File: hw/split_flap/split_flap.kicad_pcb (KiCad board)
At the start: 2 copper layers, 104.5 x 98.3 mm, 59 parts, among them J1 Conn_01x02, J10 Conn_01x05, J11 Conn_01x05, J12 Conn_01x05, J13 Conn_01x05, J14 Conn_01x05, J15 Conn_01x05, J16 Conn_01x05, J17 EXPANDER_PORT, J18 Conn_01x05, J19 POWER, J2 Conn_01x02, J20 Conn_01x05, J21 Conn_01x05, J22 Conn_01x05, J25 Conn_01x02, J26 Conn_01x02, J27 Conn_01x02, J28 Conn_01x02, J3 Conn_01x02, J4 Conn_01x02, J5 Conn_01x02, J6 Conn_01x02, J7 Conn_01x02, J8 Conn_01x02, J9 Conn_01x05, U1 PCF8574, U10 ULN2803A, U11 PCF8574, U12 ULN2803A, U13 PCF8574, U14 ULN2803A, U15 PCF8574, U2 NodeMCU_1.0_(ESP-12E), U3 PCF8574, U4 ULN2803A, U5 PCF8574, U6 ULN2803A, U7 PCF8574, U8 ULN2803A, U9 PCF8574

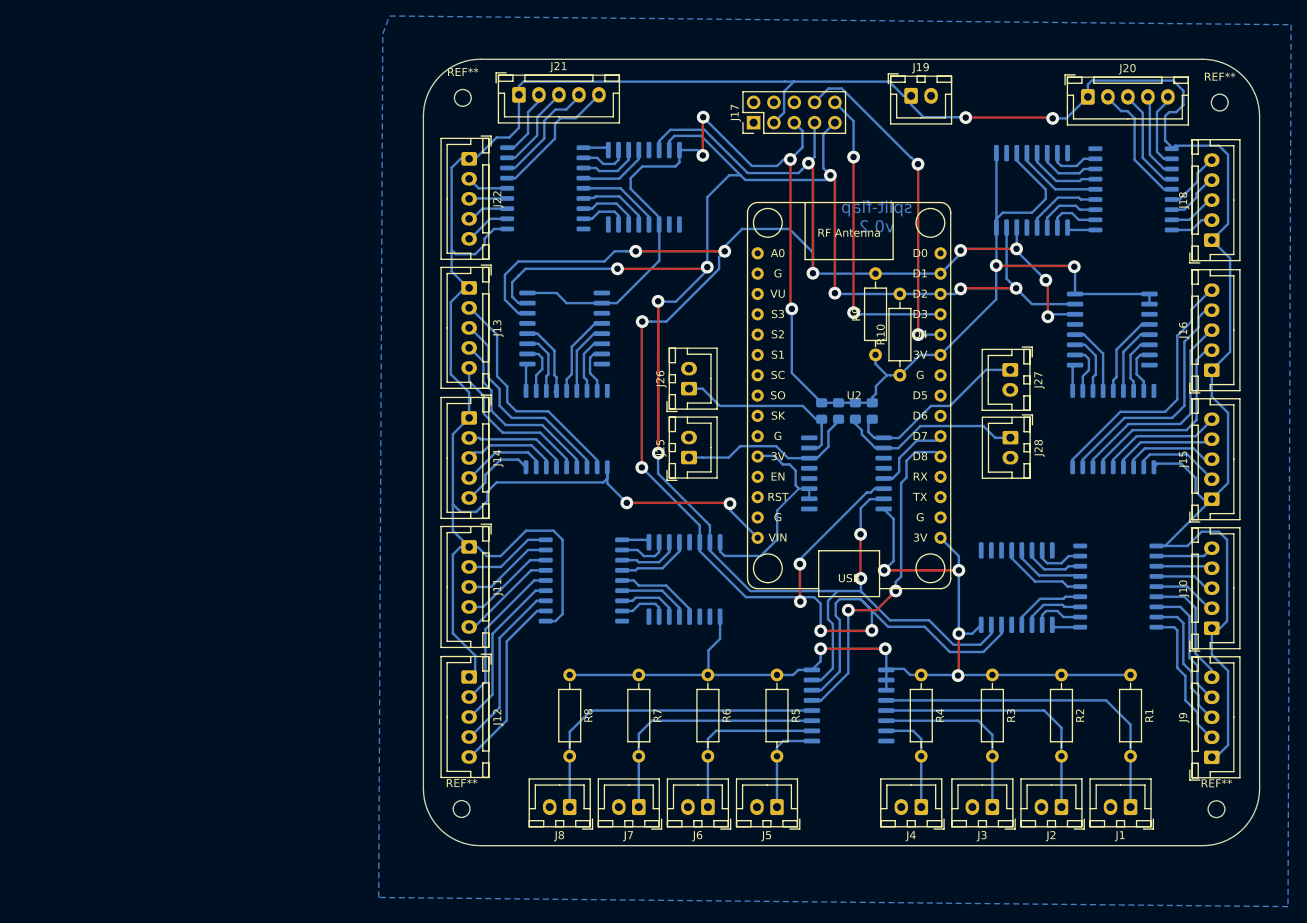
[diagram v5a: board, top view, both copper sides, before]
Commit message: Rework PCB
Start routing all expanders
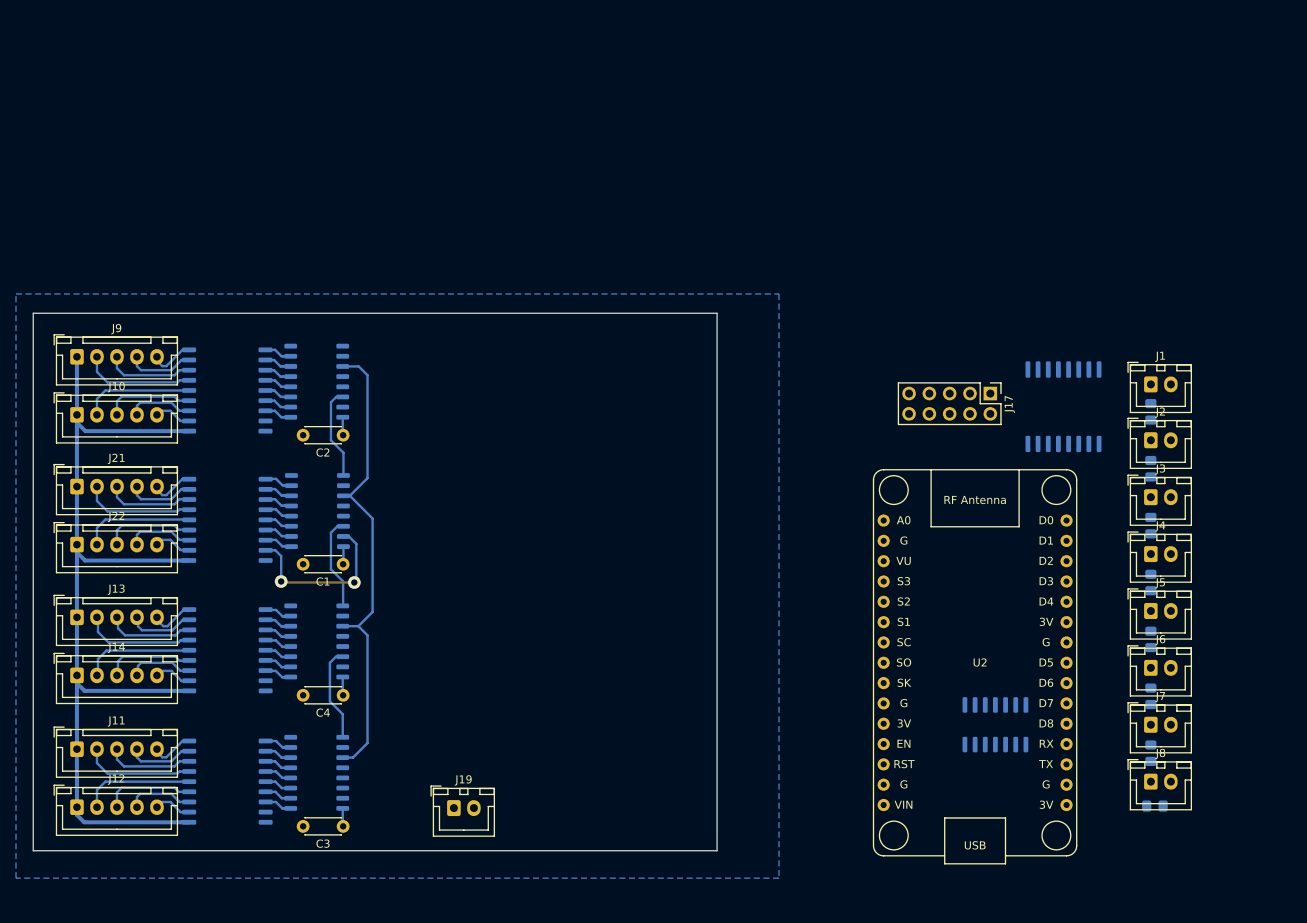
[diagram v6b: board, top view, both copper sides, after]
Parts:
- removed J15, J16, J18, J20: Conn_01x05, Connector_JST:JST_XH_B5B-XH-A_1x05_P2.50mm_Vertical
- removed J25, J26, J27, J28: Conn_01x02, Connector_JST:JST_XH_B2B-XH-A_1x02_P2.50mm_Vertical
- removed R10, R9: R, Resistor_THT:R_Axial_DIN0207_L6.3mm_D2.5mm_P10.16mm_Horizontal
- removed R13, R14, R15, R16: R, Resistor_SMD:R_0805_2012Metric_Pad1.15x1.40mm_HandSolder
- removed REF** (x4): MountingHole_2.1mm, MountingHole:MountingHole_2.1mm
- removed U11, U13, U15: PCF8574, Package_SO:SOIC-16W_7.5x10.3mm_P1.27mm
- removed U12: ULN2803A, Package_SO:SOP-18_7x12.5mm_P1.27mm
- added C1: 0.1, Capacitor_THT:C_Disc_D4.3mm_W1.9mm_P5.00mm, F.Cu at (86.4, 104.3)
- added C2: 0.1, Capacitor_THT:C_Disc_D4.3mm_W1.9mm_P5.00mm, F.Cu at (86.4, 88.1)
- added C3: 0.1, Capacitor_THT:C_Disc_D4.3mm_W1.9mm_P5.00mm, F.Cu at (86.4, 137.0)
- added C4: 0.1, Capacitor_THT:C_Disc_D4.3mm_W1.9mm_P5.00mm, F.Cu at (86.4, 120.7)
- R1, R2, R3, R4, R5, R6, R7, R8: footprint Resistor_THT:R_Axial_DIN0207_L6.3mm_D2.5mm_P10.16mm_Horizontal -> Resistor_SMD:R_0805_2012Metric_Pad1.15x1.40mm_HandSolder; moved to B.Cu
- U1: value PCF8574 -> 74HCT125; footprint Package_SO:SOIC-16W_7.5x10.3mm_P1.27mm -> Package_SO:SOIC-14_3.9x8.7mm_P1.27mm
- U3, U5, U7, U9: value PCF8574 -> 74HC595; footprint Package_SO:SOIC-16W_7.5x10.3mm_P1.27mm -> Package_SO:SOP-16_4.55x10.3mm_P1.27mm
- U4: value ULN2803A -> PCF8574; footprint Package_SO:SOP-18_7x12.5mm_P1.27mm -> Package_SO:SOIC-16W_7.5x10.3mm_P1.27mm
- moved J9 150.4 mm to (53.1, 78.3), turned to 0 degrees
- moved J10 144.3 mm to (53.1, 85.6), turned to 0 degrees
- moved U10 114.1 mm to (71.9, 115.0), turned to 180 degrees
- moved U9 106.8 mm to (83.1, 113.9), turned to 0 degrees
- moved J19 105.8 mm to (100.2, 134.7)
- moved U3 87.9 mm to (83.1, 97.6), turned to 0 degrees
- moved R8 75.0 mm to (187.8, 134.5), turned to 180 degrees
- moved J21 73.8 mm to (53.1, 94.6)
- moved J8 72.7 mm to (187.3, 131.4), turned to 0 degrees
- moved J22 68.8 mm to (53.1, 101.8), turned to 0 degrees
- moved J7 64.8 mm to (187.3, 124.3), turned to 0 degrees
- moved R7 64.8 mm to (187.3, 127.9), turned to 90 degrees
- moved J13 64.0 mm to (53.1, 110.9), turned to 0 degrees
- moved U7 63.6 mm to (83.1, 130.3), turned to 0 degrees
- moved U8 61.2 mm to (71.9, 131.4), turned to 180 degrees
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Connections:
- net Net-(J22-Pad2) renamed /sheet5DED9C19/M4
- net Net-(J22-Pad3) renamed /sheet5DED9C19/M5
- net Net-(J22-Pad4) renamed /sheet5DED9C19/M6
- net Net-(J22-Pad5) renamed /sheet5DED9C19/M7
- J10 pad 2: Net-(J10-Pad2) -> /sheet5E0964A4/M4
- J10 pad 3: Net-(J10-Pad3) -> /sheet5E0964A4/M5
- J10 pad 4: Net-(J10-Pad4) -> /sheet5E0964A4/M6
- J10 pad 5: Net-(J10-Pad5) -> /sheet5E0964A4/M7
- J11 pad 2: Net-(J11-Pad2) -> /sheet5E092C79/M3
- J11 pad 3: Net-(J11-Pad3) -> /sheet5E092C79/M2
- J11 pad 4: Net-(J11-Pad4) -> /sheet5E092C79/M1
- J11 pad 5: Net-(J11-Pad5) -> /sheet5E092C79/M0
- J12 pad 2: Net-(J12-Pad2) -> /sheet5E092C79/M4
- J12 pad 3: Net-(J12-Pad3) -> /sheet5E092C79/M5
- J12 pad 4: Net-(J12-Pad4) -> /sheet5E092C79/M6
- J12 pad 5: Net-(J12-Pad5) -> /sheet5E092C79/M7
- J13 pad 2: Net-(J13-Pad2) -> /sheet5E0B21A0/M3
- J13 pad 3: Net-(J13-Pad3) -> /sheet5E0B21A0/M2
- J13 pad 4: Net-(J13-Pad4) -> /sheet5E0B21A0/M1
- J13 pad 5: Net-(J13-Pad5) -> /sheet5E0B21A0/M0
- J14 pad 2: Net-(J14-Pad2) -> /sheet5E0B21A0/M4
- J14 pad 3: Net-(J14-Pad3) -> /sheet5E0B21A0/M5
- J14 pad 4: Net-(J14-Pad4) -> /sheet5E0B21A0/M6
- J14 pad 5: Net-(J14-Pad5) -> /sheet5E0B21A0/M7
- J17 pad 10: /EXT_INT1 -> /SPI_CLK
- J17 pad 2: GND -> /INT
- J17 pad 3: +5V -> GND
- J17 pad 4: (no net) -> /SCL
- J17 pad 5: +3V3 -> GND
- J17 pad 6: (no net) -> /SDA
- J17 pad 7: /SCL -> +5V
- J17 pad 8: /EXT_INT2 -> /SPI_CS
- J17 pad 9: /SDA -> /DI_EXP
- J21 pad 2: Net-(J21-Pad2) -> /sheet5DED9C19/M3
- J21 pad 3: Net-(J21-Pad3) -> /sheet5DED9C19/M2
- J21 pad 4: Net-(J21-Pad4) -> /sheet5DED9C19/M1
- J21 pad 5: Net-(J21-Pad5) -> /sheet5DED9C19/M0
- J9 pad 2: Net-(J9-Pad2) -> /sheet5E0964A4/M3
- J9 pad 3: Net-(J9-Pad3) -> /sheet5E0964A4/M2
- J9 pad 4: Net-(J9-Pad4) -> /sheet5E0964A4/M1
- J9 pad 5: Net-(J9-Pad5) -> /sheet5E0964A4/M0
- R1 pad 1: +3V3 -> +5V
- R2 pad 1: +3V3 -> +5V
- R3 pad 1: +3V3 -> +5V
- R4 pad 1: +3V3 -> +5V
- R5 pad 1: +3V3 -> +5V
- R6 pad 1: +3V3 -> +5V
- R7 pad 1: +3V3 -> +5V
- R8 pad 1: +3V3 -> +5V
- U1 pad 1: +3V3 -> GND
- U1 pad 10: Net-(J6-Pad1) -> GND
- U1 pad 11: Net-(J7-Pad1) -> (no net)
- U1 pad 12: Net-(J8-Pad1) -> GND
- U1 pad 13: /INT1 -> GND
- U1 pad 14: /SCL -> +5V
- U1 pad 2: +3V3 -> /SPI_3.3_CLK
- U1 pad 3: +3V3 -> /SPI_CLK
- U1 pad 4: Net-(J1-Pad1) -> GND
- U1 pad 5: Net-(J2-Pad1) -> /SPI_3.3_CS
- U1 pad 6: Net-(J3-Pad1) -> /SPI_CS
- U1 pad 7: Net-(J4-Pad1) -> GND
- U1 pad 8: GND -> /SPI_DO
- U1 pad 9: Net-(J5-Pad1) -> /SPI_3.3_DO
- U10 pad 1: /sheet5DE57FF1/L5 -> /sheet5E0B21A0/O8
- U10 pad 11: Net-(J15-Pad2) -> /sheet5E0B21A0/M7
- U10 pad 12: Net-(J15-Pad3) -> /sheet5E0B21A0/M6
- U10 pad 13: Net-(J15-Pad4) -> /sheet5E0B21A0/M5
- U10 pad 14: Net-(J15-Pad5) -> /sheet5E0B21A0/M4
- U10 pad 15: Net-(J16-Pad2) -> /sheet5E0B21A0/M3
- U10 pad 16: Net-(J16-Pad3) -> /sheet5E0B21A0/M2
- U10 pad 17: Net-(J16-Pad4) -> /sheet5E0B21A0/M1
- U10 pad 18: Net-(J16-Pad5) -> /sheet5E0B21A0/M0
- U10 pad 2: /sheet5DE57FF1/L6 -> /sheet5E0B21A0/O7
- U10 pad 3: /sheet5DE57FF1/L7 -> /sheet5E0B21A0/O6
- U10 pad 4: /sheet5DE57FF1/L8 -> /sheet5E0B21A0/O5
- U10 pad 5: /sheet5DE57FF1/L1 -> /sheet5E0B21A0/O4
- U10 pad 6: /sheet5DE57FF1/L2 -> /sheet5E0B21A0/O3
- U10 pad 7: /sheet5DE57FF1/L3 -> /sheet5E0B21A0/O2
- U10 pad 8: /sheet5DE57FF1/L4 -> /sheet5E0B21A0/O1
- U14 pad 1: /sheet5DED9C19/L5 -> /sheet5DED9C19/O8
- U14 pad 15: Net-(J21-Pad5) -> /sheet5DED9C19/M3
- U14 pad 16: Net-(J21-Pad4) -> /sheet5DED9C19/M2
- U14 pad 17: Net-(J21-Pad3) -> /sheet5DED9C19/M1
- U14 pad 18: Net-(J21-Pad2) -> /sheet5DED9C19/M0
- U14 pad 2: /sheet5DED9C19/L6 -> /sheet5DED9C19/O7
- U14 pad 3: /sheet5DED9C19/L7 -> /sheet5DED9C19/O6
- U14 pad 4: /sheet5DED9C19/L8 -> /sheet5DED9C19/O5
- U14 pad 5: /sheet5DED9C19/L1 -> /sheet5DED9C19/O4
- U14 pad 6: /sheet5DED9C19/L2 -> /sheet5DED9C19/O3
- U14 pad 7: /sheet5DED9C19/L3 -> /sheet5DED9C19/O2
- U14 pad 8: /sheet5DED9C19/L4 -> /sheet5DED9C19/O1
- U2 pad 20: /INT1 -> /SPI_3.3_DO
- U2 pad 21: /INT2 -> /SPI_3.3_CS
- U2 pad 23: (no net) -> /SPI_3.3_CLK
- U2 pad 26: /EXT_INT2 -> (no net)
- U2 pad 27: /EXT_INT1 -> /INT
- U3 pad 1: GND -> /sheet5DED9C19/O2
- U3 pad 10: /SheetMotor1/L6 -> +5V
- U3 pad 11: /SheetMotor1/L7 -> /SPI_CLK
- U3 pad 12: /SheetMotor1/L8 -> /SPI_CS
- U3 pad 13: (no net) -> GND
- U3 pad 14: /SCL -> /sheet5DED9C19/DI
- U3 pad 15: /SDA -> /sheet5DED9C19/O1
- U3 pad 16: +3V3 -> +5V
- U3 pad 2: GND -> /sheet5DED9C19/O3
- U3 pad 3: GND -> /sheet5DED9C19/O4
- U3 pad 4: /SheetMotor1/L1 -> /sheet5DED9C19/O5
- U3 pad 5: /SheetMotor1/L2 -> /sheet5DED9C19/O6
- U3 pad 6: /SheetMotor1/L3 -> /sheet5DED9C19/O7
- U3 pad 7: /SheetMotor1/L4 -> /sheet5DED9C19/O8
- U3 pad 9: /SheetMotor1/L5 -> /sheet5E0964A4/DI
- U4 pad 1: /SheetMotor1/L5 -> GND
- U4 pad 10: +5V -> Net-(J6-Pad1)
- U4 pad 11: Net-(J10-Pad5) -> Net-(J7-Pad1)
- U4 pad 12: Net-(J10-Pad4) -> Net-(J8-Pad1)
- U4 pad 13: Net-(J10-Pad3) -> /INT
- U4 pad 14: Net-(J10-Pad2) -> /SCL
- U4 pad 15: Net-(J9-Pad5) -> /SDA
- U4 pad 16: Net-(J9-Pad4) -> +5V
- U4 pad 2: /SheetMotor1/L6 -> GND
- U4 pad 3: /SheetMotor1/L7 -> GND
- U4 pad 4: /SheetMotor1/L8 -> Net-(J1-Pad1)
- U4 pad 5: /SheetMotor1/L1 -> Net-(J2-Pad1)
- U4 pad 6: /SheetMotor1/L2 -> Net-(J3-Pad1)
- U4 pad 7: /SheetMotor1/L3 -> Net-(J4-Pad1)
- U4 pad 8: /SheetMotor1/L4 -> GND
- U4 pad 9: GND -> Net-(J5-Pad1)
- U5 pad 1: +3V3 -> /sheet5E0964A4/O2
- U5 pad 10: /sheetMotor2/L6 -> +5V
- U5 pad 11: /sheetMotor2/L7 -> /SPI_CLK
- U5 pad 12: /sheetMotor2/L8 -> /SPI_CS
- U5 pad 13: (no net) -> GND
- U5 pad 14: /SCL -> /sheet5E0964A4/DI
- U5 pad 15: /SDA -> /sheet5E0964A4/O1
- U5 pad 16: +3V3 -> +5V
- U5 pad 2: GND -> /sheet5E0964A4/O3
- U5 pad 3: GND -> /sheet5E0964A4/O4
- U5 pad 4: /sheetMotor2/L1 -> /sheet5E0964A4/O5
- U5 pad 5: /sheetMotor2/L2 -> /sheet5E0964A4/O6
- U5 pad 6: /sheetMotor2/L3 -> /sheet5E0964A4/O7
- U5 pad 7: /sheetMotor2/L4 -> /sheet5E0964A4/O8
- U5 pad 9: /sheetMotor2/L5 -> /DI_EXP
- U6 pad 1: /sheetMotor2/L5 -> /sheet5E0964A4/O8
- U6 pad 11: Net-(J12-Pad5) -> /sheet5E0964A4/M7
- U6 pad 12: Net-(J12-Pad4) -> /sheet5E0964A4/M6
- U6 pad 13: Net-(J12-Pad3) -> /sheet5E0964A4/M5
- U6 pad 14: Net-(J12-Pad2) -> /sheet5E0964A4/M4
- U6 pad 15: Net-(J11-Pad5) -> /sheet5E0964A4/M3
- U6 pad 16: Net-(J11-Pad4) -> /sheet5E0964A4/M2
- U6 pad 17: Net-(J11-Pad3) -> /sheet5E0964A4/M1
- U6 pad 18: Net-(J11-Pad2) -> /sheet5E0964A4/M0
- U6 pad 2: /sheetMotor2/L6 -> /sheet5E0964A4/O7
- U6 pad 3: /sheetMotor2/L7 -> /sheet5E0964A4/O6
- U6 pad 4: /sheetMotor2/L8 -> /sheet5E0964A4/O5
- U6 pad 5: /sheetMotor2/L1 -> /sheet5E0964A4/O4
- U6 pad 6: /sheetMotor2/L2 -> /sheet5E0964A4/O3
- U6 pad 7: /sheetMotor2/L3 -> /sheet5E0964A4/O2
- U6 pad 8: /sheetMotor2/L4 -> /sheet5E0964A4/O1
- U7 pad 1: GND -> /sheet5E092C79/O2
- U7 pad 10: /Sheet5DE1D348/L6 -> +5V
- U7 pad 11: /Sheet5DE1D348/L7 -> /SPI_CLK
- U7 pad 12: /Sheet5DE1D348/L8 -> /SPI_CS
- U7 pad 13: (no net) -> GND
- U7 pad 14: /SCL -> /SPI_DO
- U7 pad 15: /SDA -> /sheet5E092C79/O1
- U7 pad 16: +3V3 -> +5V
- U7 pad 2: +3V3 -> /sheet5E092C79/O3
- U7 pad 3: GND -> /sheet5E092C79/O4
- U7 pad 4: /Sheet5DE1D348/L1 -> /sheet5E092C79/O5
- U7 pad 5: /Sheet5DE1D348/L2 -> /sheet5E092C79/O6
- U7 pad 6: /Sheet5DE1D348/L3 -> /sheet5E092C79/O7
- U7 pad 7: /Sheet5DE1D348/L4 -> /sheet5E092C79/O8
- U7 pad 9: /Sheet5DE1D348/L5 -> /sheet5E0B21A0/DI
- U8 pad 1: /Sheet5DE1D348/L5 -> /sheet5E092C79/O8
- U8 pad 11: Net-(J13-Pad2) -> /sheet5E092C79/M7
- U8 pad 12: Net-(J13-Pad3) -> /sheet5E092C79/M6
- U8 pad 13: Net-(J13-Pad4) -> /sheet5E092C79/M5
- U8 pad 14: Net-(J13-Pad5) -> /sheet5E092C79/M4
- U8 pad 15: Net-(J14-Pad2) -> /sheet5E092C79/M3
- U8 pad 16: Net-(J14-Pad3) -> /sheet5E092C79/M2
- U8 pad 17: Net-(J14-Pad4) -> /sheet5E092C79/M1
- U8 pad 18: Net-(J14-Pad5) -> /sheet5E092C79/M0
- U8 pad 2: /Sheet5DE1D348/L6 -> /sheet5E092C79/O7
- U8 pad 3: /Sheet5DE1D348/L7 -> /sheet5E092C79/O6
- U8 pad 4: /Sheet5DE1D348/L8 -> /sheet5E092C79/O5
- U8 pad 5: /Sheet5DE1D348/L1 -> /sheet5E092C79/O4
- U8 pad 6: /Sheet5DE1D348/L2 -> /sheet5E092C79/O3
- U8 pad 7: /Sheet5DE1D348/L3 -> /sheet5E092C79/O2
- U8 pad 8: /Sheet5DE1D348/L4 -> /sheet5E092C79/O1
- U9 pad 1: +3V3 -> /sheet5E0B21A0/O2
- U9 pad 10: /sheet5DE57FF1/L6 -> +5V
- U9 pad 11: /sheet5DE57FF1/L7 -> /SPI_CLK
- U9 pad 12: /sheet5DE57FF1/L8 -> /SPI_CS
- U9 pad 13: (no net) -> GND
- U9 pad 14: /SCL -> /sheet5E0B21A0/DI
- U9 pad 15: /SDA -> /sheet5E0B21A0/O1
- U9 pad 16: +3V3 -> +5V
- U9 pad 2: +3V3 -> /sheet5E0B21A0/O3
- U9 pad 3: GND -> /sheet5E0B21A0/O4
- U9 pad 4: /sheet5DE57FF1/L1 -> /sheet5E0B21A0/O5
- U9 pad 5: /sheet5DE57FF1/L2 -> /sheet5E0B21A0/O6
- U9 pad 6: /sheet5DE57FF1/L3 -> /sheet5E0B21A0/O7
- U9 pad 7: /sheet5DE57FF1/L4 -> /sheet5E0B21A0/O8
- U9 pad 9: /sheet5DE57FF1/L5 -> /sheet5DED9C19/DI
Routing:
- net +3V3: track 341.1 -> 0.00 mm, vias 12 -> 0
- net /SCL: track 275.6 -> 0.00 mm, vias 14 -> 0
- net +5V: track 388.8 -> 127.0 mm, vias 4 -> 0
- net /SDA: track 240.5 -> 0.00 mm, vias 10 -> 0
- net /SPI_CLK: track 0.00 -> 59.4 mm
- net /INT1: track 42.5 -> 0.00 mm, vias 2 -> 0
- net Net-(J1-Pad1): track 42.3 -> 0.00 mm
- net /EXT_INT2: track 41.7 -> 0.00 mm, vias 2 -> 0
- net Net-(J8-Pad1): track 41.1 -> 0.00 mm
- net /EXT_INT1: track 38.2 -> 0.00 mm, vias 2 -> 0
- net Net-(J2-Pad1): track 32.8 -> 0.00 mm
- net Net-(J16-Pad5): track 32.7 -> 0.00 mm
- net Net-(J7-Pad1): track 31.7 -> 0.00 mm
- net Net-(J16-Pad4): track 30.3 -> 0.00 mm
- net Net-(J13-Pad2): track 29.0 -> 0.00 mm
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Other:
- board size 104.5 x 98.3 mm -> 85.5 x 67.2 mm
- board text removed: "split-flap v0.2"

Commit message: Route new PCB completely.
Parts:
- added REF**: OSHW-Logo_7.5x8mm_Copper, Symbol:OSHW-Logo_7.5x8mm_Copper, B.Cu at (153.5, 92.9)
- added REF**: MountingHole_3.2mm_M3, MountingHole:MountingHole_3.2mm_M3, F.Cu at (180.1, 127.0)
- added REF**: MountingHole_3.2mm_M3, MountingHole:MountingHole_3.2mm_M3, F.Cu at (100.0, 127.0)
- added REF**: MountingHole_3.2mm_M3, MountingHole:MountingHole_3.2mm_M3, F.Cu at (180.1, 60.0)
- added REF**: MountingHole_3.2mm_M3, MountingHole:MountingHole_3.2mm_M3, F.Cu at (100.0, 60.0)
- moved J19 86.8 mm to (150.9, 64.3)
- moved J11 62.4 mm to (114.2, 114.7), turned to 180 degrees
- moved J9 62.3 mm to (114.2, 66.0), turned to 180 degrees
- moved J13 62.3 mm to (114.2, 98.6), turned to 180 degrees
- moved J12 62.3 mm to (114.2, 122.4), turned to 180 degrees
- moved J21 62.3 mm to (114.2, 82.3), turned to 180 degrees
- moved J10 62.2 mm to (114.2, 73.6), turned to 180 degrees
- moved J22 62.2 mm to (114.2, 89.9), turned to 180 degrees
- moved J14 62.2 mm to (114.2, 106.3), turned to 180 degrees
- moved C1 52.5 mm to (137.4, 92.0)
- moved C2 52.5 mm to (137.4, 75.9)
- moved C3 52.5 mm to (137.4, 124.8)
- moved C4 52.5 mm to (137.4, 108.4)
- moved U10 52.5 mm to (122.9, 102.8)
- moved U14 52.5 mm to (122.9, 86.5)
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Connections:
- J10 pad 1: +5V -> /sheet5E0964A4/M7
- J10 pad 2: /sheet5E0964A4/M4 -> /sheet5E0964A4/M6
- J10 pad 4: /sheet5E0964A4/M6 -> /sheet5E0964A4/M4
- J10 pad 5: /sheet5E0964A4/M7 -> +5V
- J11 pad 1: +5V -> /sheet5E092C79/M0
- J11 pad 2: /sheet5E092C79/M3 -> /sheet5E092C79/M1
- J11 pad 4: /sheet5E092C79/M1 -> /sheet5E092C79/M3
- J11 pad 5: /sheet5E092C79/M0 -> +5V
- J12 pad 1: +5V -> /sheet5E092C79/M7
- J12 pad 2: /sheet5E092C79/M4 -> /sheet5E092C79/M6
- J12 pad 4: /sheet5E092C79/M6 -> /sheet5E092C79/M4
- J12 pad 5: /sheet5E092C79/M7 -> +5V
- J13 pad 1: +5V -> /sheet5E0B21A0/M0
- J13 pad 2: /sheet5E0B21A0/M3 -> /sheet5E0B21A0/M1
- J13 pad 4: /sheet5E0B21A0/M1 -> /sheet5E0B21A0/M3
- J13 pad 5: /sheet5E0B21A0/M0 -> +5V
- J14 pad 1: +5V -> /sheet5E0B21A0/M7
- J14 pad 2: /sheet5E0B21A0/M4 -> /sheet5E0B21A0/M6
- J14 pad 4: /sheet5E0B21A0/M6 -> /sheet5E0B21A0/M4
- J14 pad 5: /sheet5E0B21A0/M7 -> +5V
- J21 pad 1: +5V -> /sheet5DED9C19/M0
- J21 pad 2: /sheet5DED9C19/M3 -> /sheet5DED9C19/M1
- J21 pad 4: /sheet5DED9C19/M1 -> /sheet5DED9C19/M3
- J21 pad 5: /sheet5DED9C19/M0 -> +5V
- J22 pad 1: +5V -> /sheet5DED9C19/M7
- J22 pad 2: /sheet5DED9C19/M4 -> /sheet5DED9C19/M6
- J22 pad 4: /sheet5DED9C19/M6 -> /sheet5DED9C19/M4
- J22 pad 5: /sheet5DED9C19/M7 -> +5V
- J9 pad 1: +5V -> /sheet5E0964A4/M0
- J9 pad 2: /sheet5E0964A4/M3 -> /sheet5E0964A4/M1
- J9 pad 4: /sheet5E0964A4/M1 -> /sheet5E0964A4/M3
- J9 pad 5: /sheet5E0964A4/M0 -> +5V
- U2 pad 20: /SPI_3.3_DO -> /SPI_3.3_CS
- U2 pad 21: /SPI_3.3_CS -> /SPI_3.3_DO
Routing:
- net +5V: track 127.0 -> 445.7 mm, vias 0 -> 14
- net /SPI_CS: track 0.00 -> 101.3 mm, vias 0 -> 8
- net Net-(J8-Pad1): track 0.00 -> 51.2 mm
- net /INT: track 0.00 -> 44.5 mm, vias 0 -> 2
- net Net-(J7-Pad1): track 0.00 -> 42.8 mm
- net /SDA: track 0.00 -> 42.6 mm
- net Net-(J6-Pad1): track 0.00 -> 35.2 mm
- net /SPI_CLK: track 59.4 -> 93.6 mm
- net Net-(J1-Pad1): track 0.00 -> 31.2 mm
- net /SPI_3.3_CLK: track 0.00 -> 30.8 mm
- net /SCL: track 0.00 -> 26.9 mm
- net Net-(J5-Pad1): track 0.00 -> 26.7 mm
- net Net-(J2-Pad1): track 0.00 -> 24.3 mm
- net /SPI_DO: track 0.00 -> 23.1 mm
- net /sheet5E0B21A0/O1: track 0.00 -> 22.3 mm, vias 0 -> 2
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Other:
- board size 85.5 x 67.2 mm -> 90 x 77.1 mm

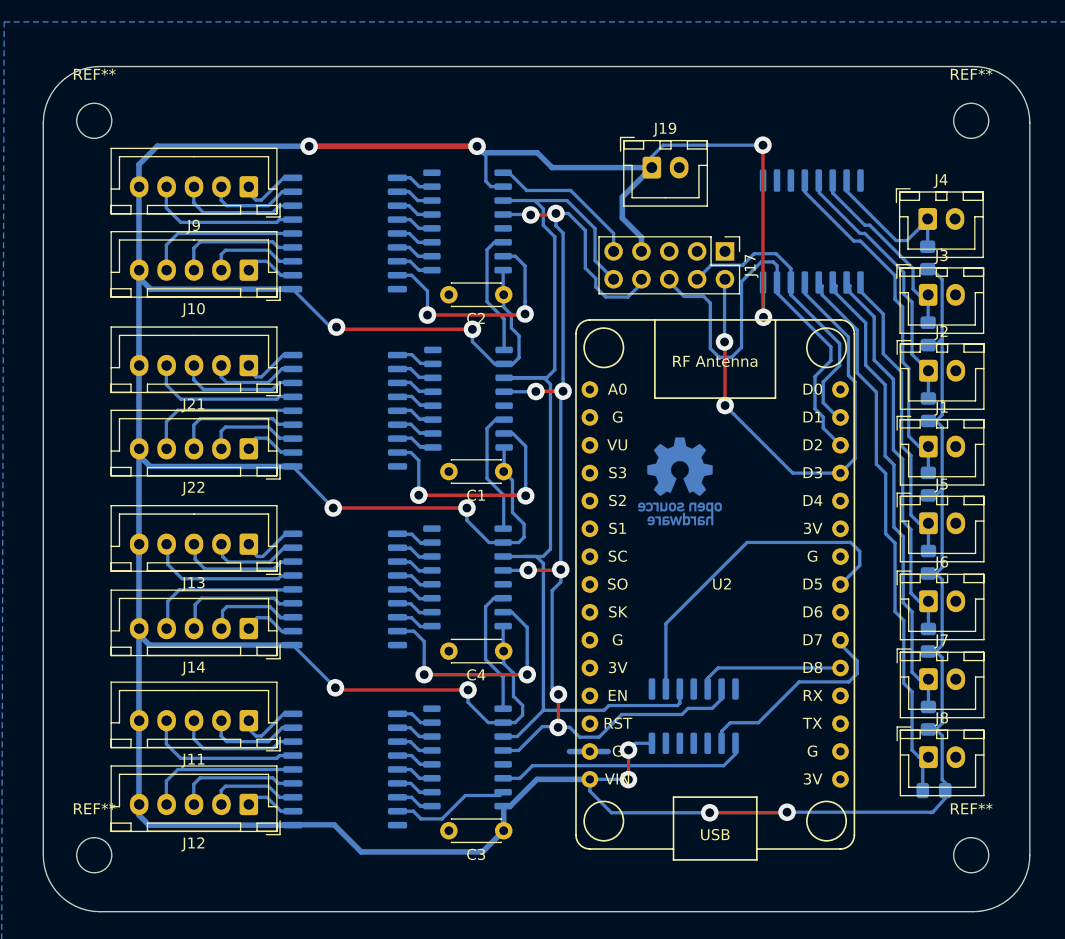
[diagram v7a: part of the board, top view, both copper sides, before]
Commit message: Add VCC for motors
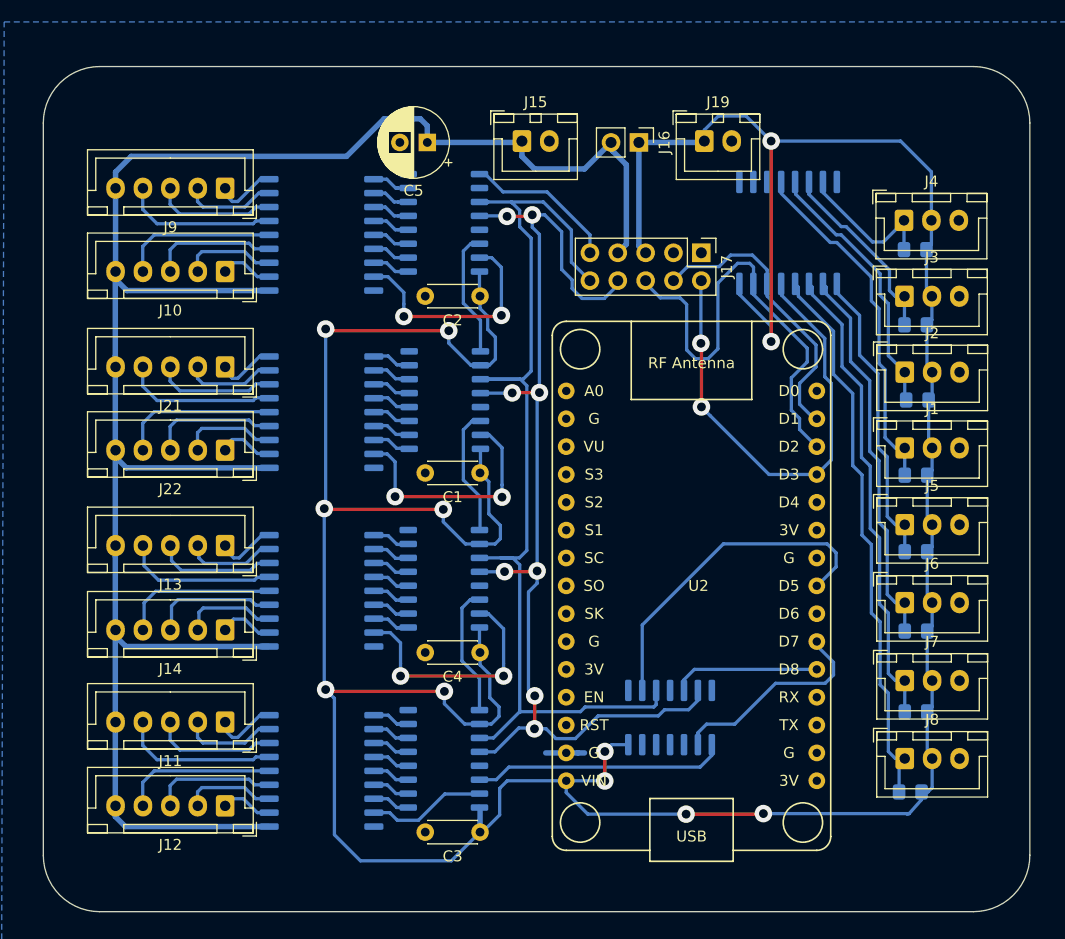
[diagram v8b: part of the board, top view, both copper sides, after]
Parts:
- removed REF**: OSHW-Logo_7.5x8mm_Copper, Symbol:OSHW-Logo_7.5x8mm_Copper
- removed REF** (x4): MountingHole_3.2mm_M3, MountingHole:MountingHole_3.2mm_M3
- added C5: CP, Capacitor_THT:CP_Radial_D6.3mm_P2.50mm, F.Cu at (130.4, 62.0)
- added J15: MOTOR_POWER, Connector_JST:JST_XH_B2B-XH-A_1x02_P2.50mm_Vertical, F.Cu at (139.1, 61.8)
- added J16: JUMPER_MOTOR_5V, Connector_PinHeader_2.54mm:PinHeader_1x02_P2.54mm_Vertical, F.Cu at (149.7, 62.0)
- J1, J2, J3, J4, J5, J6, J7, J8: footprint Connector_JST:JST_XH_B2B-XH-A_1x02_P2.50mm_Vertical -> Connector_JST:JST_XH_B3B-XH-A_1x03_P2.50mm_Vertical
- moved J19 5.37 mm to (155.7, 61.8)
- moved U4 2.16 mm to (163.3, 70.2)
- moved J11 2.16 mm to (112.0, 114.9)
- moved J22 2.16 mm to (112.0, 90.1)
- moved J10 2.16 mm to (112.0, 73.8)
- moved J12 2.16 mm to (112.0, 122.5)
- moved J13 2.16 mm to (112.0, 98.8)
- moved J14 2.16 mm to (112.0, 106.5)
- moved J21 2.16 mm to (112.0, 82.5)
- moved J9 2.16 mm to (112.0, 66.2)
- moved C2 2.16 mm to (135.2, 76.0)
- moved C4 2.16 mm to (135.2, 108.5)
- moved J17 2.16 mm to (155.4, 72.0)
- moved J2 2.16 mm to (174.0, 82.9)
- moved J4 2.16 mm to (173.9, 69.1)
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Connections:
- J1 pad 2: GND -> +5V
- J10 pad 5: +5V -> VCC
- J11 pad 5: +5V -> VCC
- J12 pad 5: +5V -> VCC
- J13 pad 5: +5V -> VCC
- J14 pad 5: +5V -> VCC
- J17 pad 5: GND -> +5V
- J17 pad 7: +5V -> VCC
- J2 pad 2: GND -> +5V
- J21 pad 5: +5V -> VCC
- J22 pad 5: +5V -> VCC
- J3 pad 2: GND -> +5V
- J4 pad 2: GND -> +5V
- J5 pad 2: GND -> +5V
- J6 pad 2: GND -> +5V
- J7 pad 2: GND -> +5V
- J8 pad 2: GND -> +5V
- J9 pad 5: +5V -> VCC
- U10 pad 10: +5V -> VCC
- U14 pad 10: +5V -> VCC
- U6 pad 10: +5V -> VCC
- U8 pad 10: +5V -> VCC
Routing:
- net VCC: track 0.00 -> 182.7 mm
- net +5V: track 445.7 -> 325.6 mm, vias 14 -> 12
